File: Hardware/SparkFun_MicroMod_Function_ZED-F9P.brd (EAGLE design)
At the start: 160 x 100 mm, 0 parts

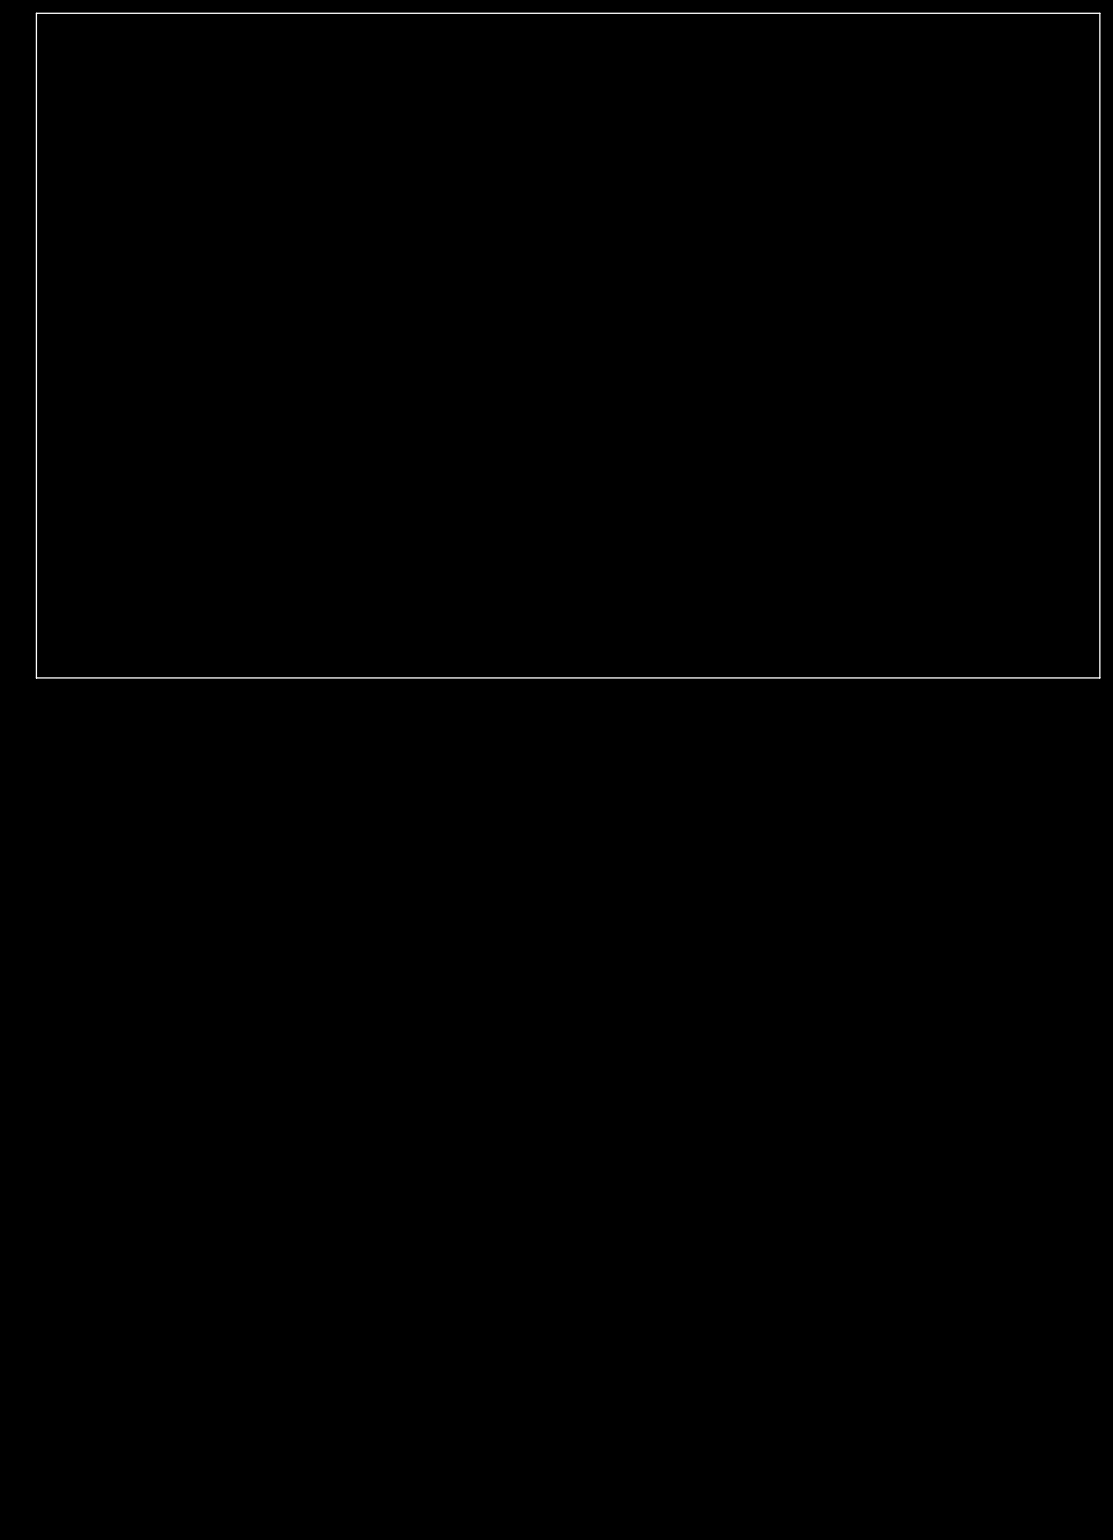
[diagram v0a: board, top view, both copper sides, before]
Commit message: Added EEPROM. Added LEDs. Added Module. Added Backup Battery. Added USB-C connector. Added Qwiic connector. Added GNSS App Note.
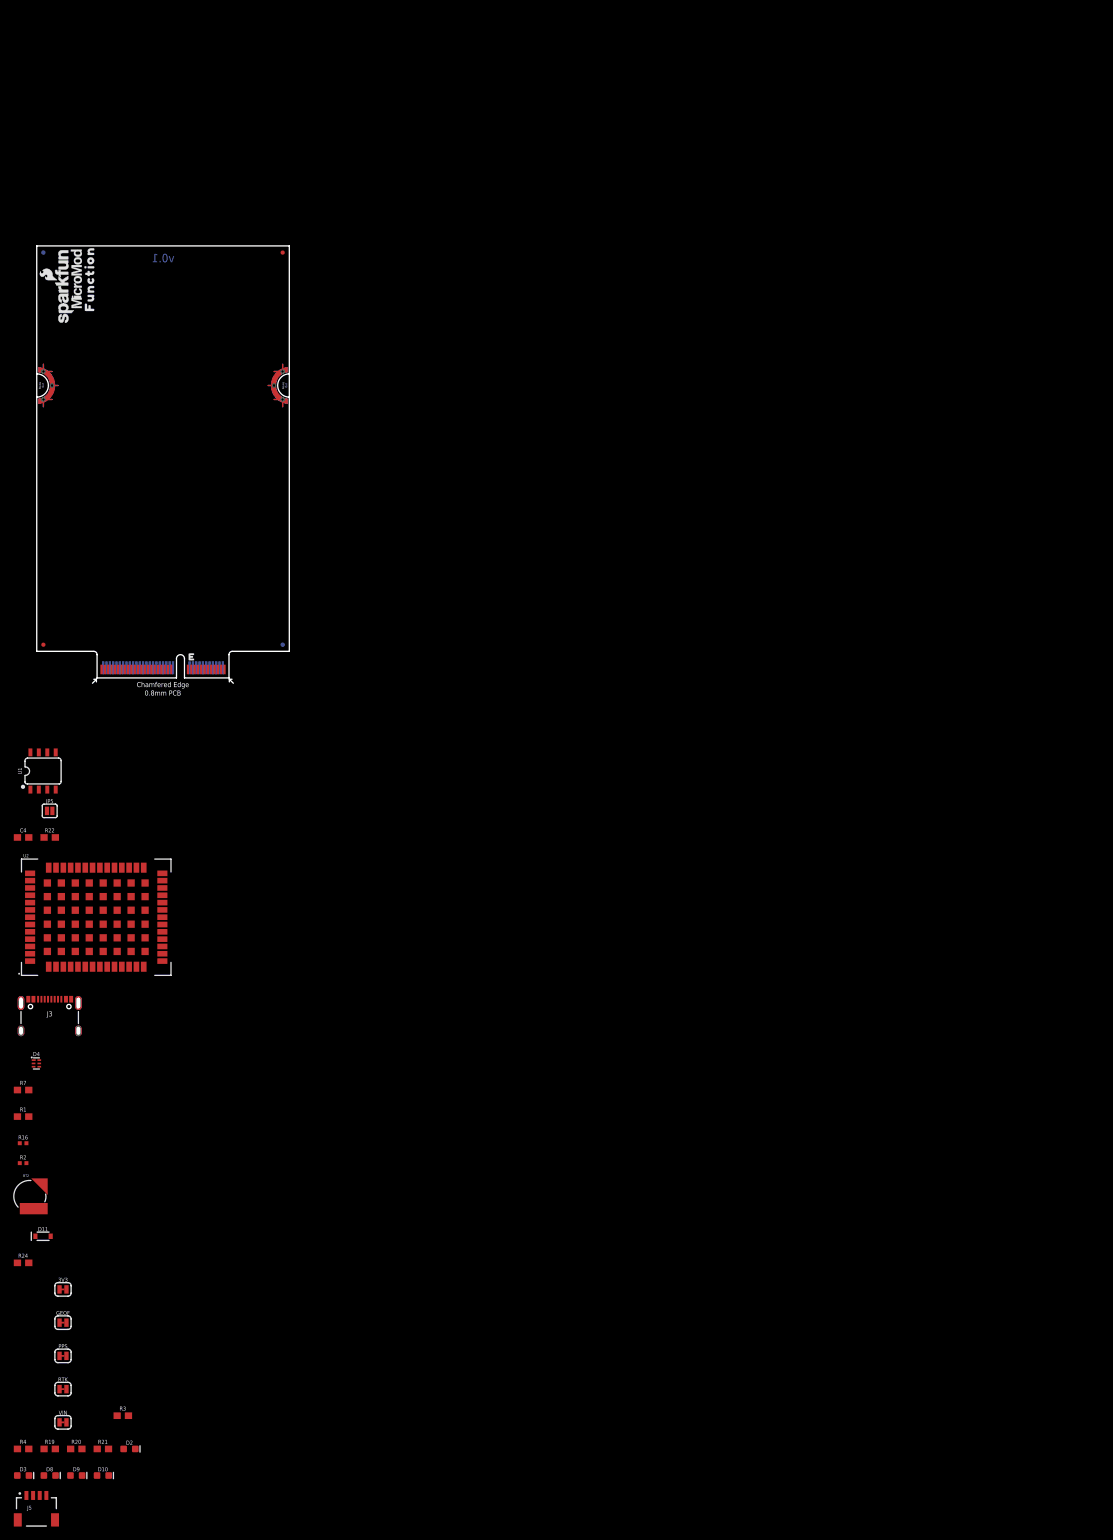
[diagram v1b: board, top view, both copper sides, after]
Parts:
- added 3V3, GEOF, PPS, RTK, VIN: JUMPER-SMT_2_NC_TRACE_SILK, SparkFun-Jumpers:SMT-JUMPER_2_NC_TRACE_SILK
- added BT2: ML414H_IV01E_BATTERY, SparkFun-Batteries:ML414H_IV01E
- added C4: 0.1uF, SparkFun-Capacitors:0603
- added D10, D8, D9: BLUE, SparkFun-LED:LED-0603
- added D11: 0.5A/40V/420mV, SparkFun-DiscreteSemi:SOD-323
- added D2, D3: RED, SparkFun-LED:LED-0603
- added D4: PRTR5V0U2F, SparkFun-IC-Power:SOT886
- added FD1, FD2, FD3, FD4: FIDUCIALUFIDUCIAL, SparkFun-Aesthetics:FIDUCIAL-MICRO
- added FRAME1: FRAME-LEDGER, SparkFun-Aesthetics:CREATIVE_COMMONS
- added J11: MICROMOD_STANDARD, SparkFun-MicroMod-Function:M.2-CARD-E-22_FUNCTION_STANDARD
- added J3: (no value), SparkFun-Connectors:USB-C-16P-2LAYER-PADS
- added J5: QWIIC_RA, SparkFun-Connectors:JST04_1MM_RA
- added JP5: JUMPER-SMT_2_NO_SILK, SparkFun-Jumpers:SMT-JUMPER_2_NO_SILK
- added LOGO1, LOGO4: SFE_LOGO_NAME_FLAME.1_INCH, SparkFun-Aesthetics:SFE_LOGO_NAME_FLAME_.1
- added LOGO2: SPECIAL_INSTRUCTIONS-ORDERING, SparkFun-Aesthetics:ORDERING_INSTRUCTIONS
- added LOGO3: OSHW-LOGOMINI, SparkFun-Aesthetics:OSHW-LOGO-MINI
- added R1, R7: 5.1k, SparkFun-Resistors:0603
- added R16, R2: 27OHM, SparkFun-Resistors:0402-TIGHT
- added R19, R20, R21, R3, R4: 1k, SparkFun-Resistors:0603
- added R22: 10k, SparkFun-Resistors:0603@1
- added R24: 3.3k, SparkFun-Resistors:0603
- added U$26, U$27: (no value), output:FUNCTION0
- added U$37, U$63: (no value), SparkFun-MicroMod:MICROMOD_LOGO_.35
- added U1: EEPROM, SparkFun-IC-Memory:SO08
- added U2: U-BLOX_ZED-F9P, SparkFun-GPS:ZED-F9P
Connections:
- new net 3.3V: C4.1, D11.A, D2.A, J11.73, J5.2, R22.1, U1.8
- new net A0: J11.36, U1.1
- new net A1: J11.34, U1.2
- new net A2: J11.32, U1.3
- new net EWP: J11.40, JP5.2, R22.2, U1.7
- new net GEO_STAT: D10.A
- new net GND: 3V3.2, BT2.-, C4.2, D4.2, GEOF.1, J11.1, J11.33, J11.39, J11.45, J11.75, J11.GND1, J11.GND2, J11.GND3, J11.GND4, J11.GND5, J11.GND6, J3.GND, J3.GND2, J5.1, JP5.1, PPS.1, R1.1, R7.1, RTK.1, U1.4, U2.1, U2.100, U2.101, U2.102, U2.12, U2.14, U2.3, U2.32, U2.37, U2.41, U2.48, U2.55, U2.56, U2.57, U2.58, U2.59, U2.60, U2.61, U2.62, U2.63, U2.64, U2.65, U2.66, U2.67, U2.68, U2.69, U2.70, U2.71, U2.72, U2.73, U2.74, U2.75, U2.76, U2.77, U2.78, U2.79, U2.80, U2.81, U2.82, U2.83, U2.84, U2.85, U2.86, U2.87, U2.88, U2.89, U2.90, U2.91, U2.92, U2.93, U2.94, U2.95, U2.96, U2.97, U2.98, U2.99, VIN.2
- new net N$1: D4.1, J3.A6, J3.B6
- new net N$10: R4.1, VIN.1
- new net N$11: D3.C, R4.2
- new net N$2: D4.3, J3.A7, J3.B7
- new net N$27: PPS.2, R19.1
- new net N$28: D8.C, R19.2
- new net N$29: D9.C, R20.2
- new net N$3: J3.B5, R7.2
- new net N$32: D11.C, R24.2
- new net N$4: J3.A5, R1.2
- new net N$45: GEOF.2, R21.1
- new net N$46: D10.C, R21.2
- new net N$5: D4.6, R16.1
- new net N$6: D4.4, R2.1
- new net N$7: D2.C, R3.2
- new net N$8: R20.1, RTK.2
- new net N$9: 3V3.1, R3.1
- new net PPS: D8.A
- new net PWR_EN: J11.71
- new net RTK_STAT: D9.A
- new net SCL/SCK: J11.21, J5.4, U1.6
- new net SDA/!CS!: J11.19, J5.3, U1.5
- new net SPI_CIPO: J11.7
- new net SPI_COPI: J11.5
- new net SPI_SCK: J11.3
- new net VCC: J11.72, J11.74
- new net VIN: D3.A
- new net V_BATT: BT2.+, R24.1
- new net V_USB: D4.5, J3.VBUS1, J3.VBUS2
- new net ZED_USB_N: R2.2
- new net ZED_USB_P: R16.2
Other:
- board size 160 x 100 mm -> 38 x 65 mm
- board text added: "2-Layer"
- board text added: "A. Brudner"
- board text added: "Beveled Edge"
- board text added: "Board Thickness is 0.8mm"
- board text added: "Dimensions are in mm"
- board text added: "ENIG Finish"
- board text added: "v0.1"

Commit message: Added I2C protection for ZED_F9P
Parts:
- added R5: 10k, SparkFun-Resistors:0603
- added U3: (no value), SparkFun-IC-Comms:SOP50P310X90-8L
- R22: device SparkFun-Resistors:0603@1 -> SparkFun-Resistors:0603
- moved GEOF 213.6 mm to (-0.52, -310.6)
- moved PPS 195.9 mm to (-0.52, -297.9)
- moved RTK 178.2 mm to (-0.52, -285.1)
- moved 3V3 167.8 mm to (-0.52, -259.8)
- moved VIN 160.5 mm to (-0.52, -272.4)
- moved R21 131.5 mm to (-0.85, -247.1)
- moved R22 121.5 mm to (-0.85, -145.4)
- moved R20 118.5 mm to (-0.85, -234.3)
- moved R19 105.7 mm to (-0.85, -221.7)
- moved R1 104.9 mm to (-0.85, -170.8)
- moved R7 96.2 mm to (-0.85, -158.2)
- moved R24 95.6 mm to (-0.85, -183.6)
- moved R4 93.0 mm to (-0.85, -208.9)
- moved R3 86.4 mm to (-0.85, -196.2)
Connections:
- new net ZED_SCL/SCK: U2.45, U3.6
- new net ZED_SDA/!CS!: U2.44, U3.5
- net 3.3V: now also R5.2, U3.2, U3.7, U3.8
- net GND: now also R5.1, U3.1
- net SCL/SCK: now also U3.3
- net SDA/!CS!: now also U3.4

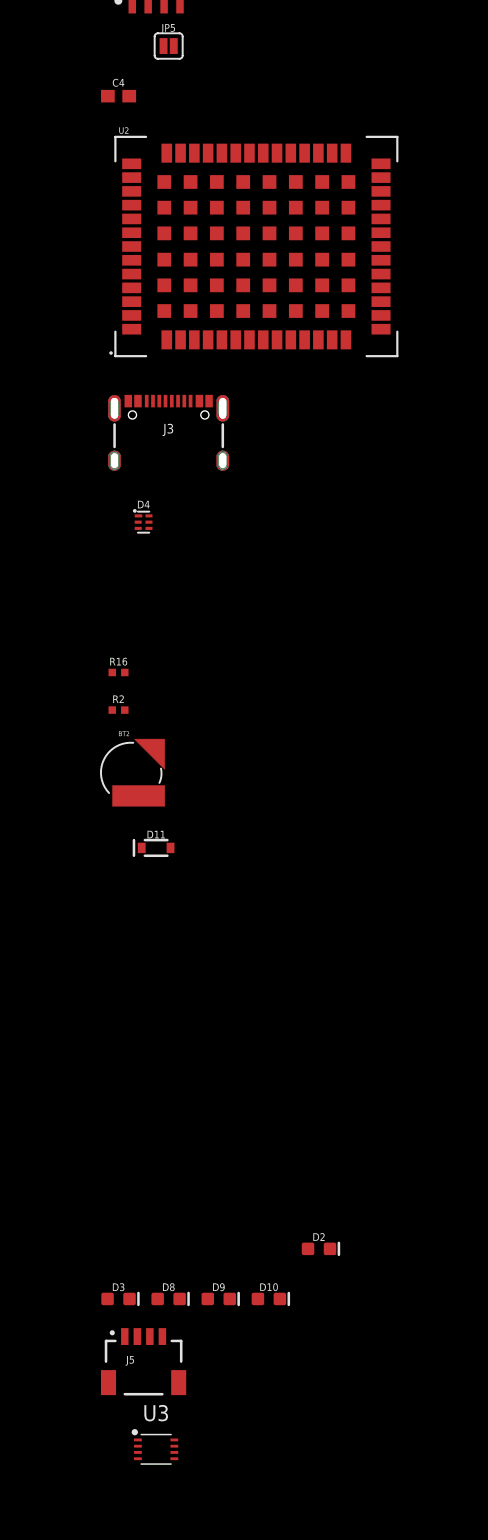
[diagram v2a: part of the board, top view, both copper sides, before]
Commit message: Created local library. Added ZED-F9P to sch.
Created Local library.
Added inverter to lib.
Added octal buffer to lib.
Added modified ZED-F9P to lib.
Added ZED-F9P to sch.
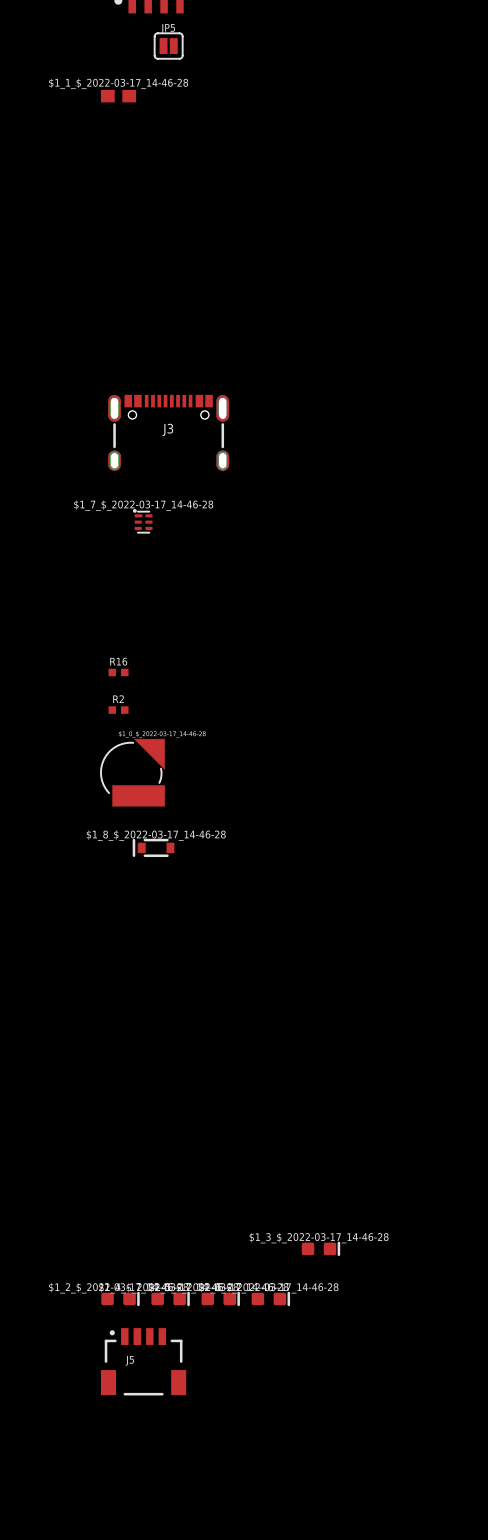
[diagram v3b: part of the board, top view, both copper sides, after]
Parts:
- removed U2: U-BLOX_ZED-F9P, SparkFun-GPS:ZED-F9P
- removed U3: (no value), SparkFun-IC-Comms:SOP50P310X90-8L
- renumbered BT2 to $1_0_$_2022-03-17_14-46-28, C4 to $1_1_$_2022-03-17_14-46-28, D10 to $1_6_$_2022-03-17_14-46-28, D11 to $1_8_$_2022-03-17_14-46-28, D2 to $1_3_$_2022-03-17_14-46-28, D3 to $1_2_$_2022-03-17_14-46-28, D4 to $1_7_$_2022-03-17_14-46-28, D8 to $1_4_$_2022-03-17_14-46-28, D9 to $1_5_$_2022-03-17_14-46-28, FD1 to $1_9_$_2022-03-17_14-46-28, FD2 to $1_11_$_2022-03-17_14-46-28, FD3 to $1_12_$_2022-03-17_14-46-28, FD4 to $1_10_$_2022-03-17_14-46-28, FRAME1 to $1_13_$_2022-03-17_14-46-28
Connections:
- removed net ZED_SCL/SCK: U2.45, U3.6
- removed net ZED_SDA/!CS!: U2.44, U3.5
- net 3.3V: no longer U3.2, U3.7, U3.8
- net GND: no longer U2.1, U2.100, U2.101, U2.102, U2.12, U2.14, U2.3, U2.32, U2.37, U2.41, U2.48, U2.55, U2.56, U2.57, U2.58, U2.59, U2.60, U2.61, U2.62, U2.63, U2.64, U2.65, U2.66, U2.67, U2.68, U2.69, U2.70, U2.71, U2.72, U2.73, U2.74, U2.75, U2.76, U2.77, U2.78, U2.79, U2.80, U2.81, U2.82, U2.83, U2.84, U2.85, U2.86, U2.87, U2.88, U2.89, U2.90, U2.91, U2.92, U2.93, U2.94, U2.95, U2.96, U2.97, U2.98, U2.99, U3.1
- net SCL/SCK: no longer U3.3
- net SDA/!CS!: no longer U3.4

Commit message: Filled out octal buffers, labeled nets. Modified inverter sch symbol.
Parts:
- removed $1_0_$_2022-03-17_14-46-28: ML414H_IV01E_BATTERY, SparkFun-Batteries:ML414H_IV01E
- removed $1_1_$_2022-03-17_14-46-28: 0.1uF, SparkFun-Capacitors:0603
- removed $1_2_$_2022-03-17_14-46-28, $1_3_$_2022-03-17_14-46-28: RED, SparkFun-LED:LED-0603
- removed $1_4_$_2022-03-17_14-46-28, $1_5_$_2022-03-17_14-46-28, $1_6_$_2022-03-17_14-46-28: BLUE, SparkFun-LED:LED-0603
- removed $1_7_$_2022-03-17_14-46-28: PRTR5V0U2F, SparkFun-IC-Power:SOT886
- removed $1_8_$_2022-03-17_14-46-28: 0.5A/40V/420mV, SparkFun-DiscreteSemi:SOD-323
- removed J5: QWIIC_RA, SparkFun-Connectors:JST04_1MM_RA
- removed R19, R21: 1k, SparkFun-Resistors:0603
- removed R22: 10k, SparkFun-Resistors:0603
- removed RTK: JUMPER-SMT_2_NC_TRACE_SILK, SparkFun-Jumpers:SMT-JUMPER_2_NC_TRACE_SILK
- added BT1: ML414H_IV01E_BATTERY, SparkFun-Batteries:ML414H_IV01E
- added C1: 10pF, SparkFun-Capacitors:0603
- added C2: 0.1uF, SparkFun-Capacitors:0603
- added D1, D2: RED, SparkFun-LED:LED-0603
- added D3, D4, D5: BLUE, SparkFun-LED:LED-0603
- added D6: PRTR5V0U2F, SparkFun-IC-Power:SOT886
- added D7: 0.5A/40V/420mV, SparkFun-DiscreteSemi:SOD-323
- added J1: (no value), SparkFun-Connectors:USB-C-16P-2LAYER-PADS
- added JP1: JUMPER-SMT_2_NO_SILK, SparkFun-Jumpers:SMT-JUMPER_2_NO_SILK
- added JP7: NC, SparkFun-Jumpers:SMT-JUMPER_2_NC_TRACE_SILK
- added R10, R9: 27OHM, SparkFun-Resistors:0402-TIGHT
- added R12: 220k, SparkFun-Resistors:0603
- added R13, R14, R15: 1.5k, SparkFun-Resistors:0603
- added R17: 10k, SparkFun-Resistors:0603
- added R8: 5.1k, SparkFun-Resistors:0603
- added U2: PCA9306DCUR, MicroMod_Function_GNSS_ublox_ZED-F9P:VSSOP-8_DCU
- added U3: U-BLOX_ZED-F9P, MicroMod_Function_GNSS_ublox_ZED-F9P:ZED-F9P
- added U4, U5: 74LVC541ABQ, MicroMod_Function_GNSS_ublox_ZED-F9P:DHVQFN20
- added U6: SN74AUP1T04DCK, MicroMod_Function_GNSS_ublox_ZED-F9P:SC-70-5_DCK
- J3: value (none) -> QWIIC_RA; device SparkFun-Connectors:USB-C-16P-2LAYER-PADS -> SparkFun-Connectors:JST04_1MM_RA
- JP5: value JUMPER-SMT_2_NO_SILK -> JUMPER-SMT_2_NC_TRACE_SILK; device SparkFun-Jumpers:SMT-JUMPER_2_NO_SILK -> SparkFun-Jumpers:SMT-JUMPER_2_NC_TRACE_SILK
- R1: value 5.1k -> 10k
- R16: value 27OHM -> 1.5k; device SparkFun-Resistors:0402-TIGHT -> SparkFun-Resistors:0603
- R2: value 27OHM -> 5.1k; device SparkFun-Resistors:0402-TIGHT -> SparkFun-Resistors:0603
- R5: value 10k -> 1k
- R7: value 5.1k -> 1k
- moved R16 314.5 mm to (-19.0, -384.0)
- moved JP5 265.2 mm to (-0.52, -285.1)
- moved R5 93.4 mm to (-0.85, -221.7)
- moved R7 88.9 mm to (-0.85, -247.1)
- moved R2 85.2 mm to (-0.85, -158.2)
- moved J3 75.0 mm to (0.00, -123.0)
- moved R1 25.4 mm to (-0.85, -145.4)
- moved R3 12.7 mm to (-0.85, -208.9)
- moved R4 12.7 mm to (-0.85, -196.2)
- renumbered $1_10_$_2022-03-17_14-46-28 to FD2, $1_11_$_2022-03-17_14-46-28 to FD3, $1_12_$_2022-03-17_14-46-28 to FD4, $1_13_$_2022-03-17_14-46-28 to FRAME1, $1_9_$_2022-03-17_14-46-28 to FD1, 3V3 to JP3, GEOF to JP6, J11 to J2, PPS to JP4, R20 to R6, R24 to R11, VIN to JP2
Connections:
- removed net SPI_CIPO: J2.7
- removed net SPI_COPI: J2.5
- removed net SPI_SCK: J2.3
- new net !RESET!: U4.P$4
- new net !SAFEBOOT!: U4.P$5
- new net !SHORT!: U4.P$8
- new net ANT_DETECT: U4.P$7
- new net ANT_OFF: U5.P$18
- new net EXTINT: U4.P$6
- new net IO_!OE!: U4.P$1, U4.P$19, U5.P$1, U5.P$19, U6.P$4
- new net N$12: C1.1, R12.1, U2.P$7, U2.P$8
- new net N$13: C2.1, U1.8
- new net N$14: U6.P$2, U6.P$5
- new net N$16: JP7.2
- new net N$18: J2.38
- new net N$19: J2.47
- new net N$21: J2.51
- new net N$22: J2.53
- new net N$23: J2.55
- new net N$24: JP7.1, R17.2, U4.P$9
- new net N$25: J2.57
- new net N$26: J2.59
- new net N$30: J2.61
- new net N$31: J2.70
- new net N$33: J2.37
- new net N$34: J2.35
- new net N$35: J2.18
- new net N$36: J2.16
- new net N$37: J2.43
- new net N$38: J2.41
- new net N$39: U4.P$20
- new net N$42: U5.P$20
- new net N$69: U3.38
- new net N$73: U3.7
- new net N$74: U3.2
- new net N$77: U3.33, U3.34
- new net RX/COPI: J2.15, J2.5, U4.P$3
- new net RX2/RTCM: U4.P$2
- new net TIMEPULSE: U5.P$12
- new net TX/CIPO: J2.13, J2.7, U5.P$14
- new net TX2/RTCM: U5.P$15
- new net TX_READY: J2.23, U5.P$13
- new net ZED_!ANT_SHORT!: U3.6
- new net ZED_!RESET!: U3.49, U4.P$16
- new net ZED_!SAFEBOOT!: U3.50, U4.P$15
- new net ZED_!SHORT!: U4.P$12
- new net ZED_ANT_DETECT: U3.4, U4.P$13
- new net ZED_ANT_OFF: U3.5, U5.P$2
- new net ZED_DSEL: U3.47, U4.P$11
- new net ZED_EXTINT: U3.51, U4.P$14
- new net ZED_GEO_STAT: U3.19, U5.P$3
- new net ZED_RTK_STAT: U3.20, U5.P$4
- new net ZED_RX/COPI: U3.43, U4.P$17
- new net ZED_RX2/RTCM: U3.26, U4.P$18
- new net ZED_SCL/SCK: R14.1, U2.P$6, U3.45
- new net ZED_SDA/!CS!: R13.1, U2.P$5, U3.44
- new net ZED_TIMEPULSE: U3.53, U5.P$8
- new net ZED_TX/CIPO: U3.42, U5.P$6
- new net ZED_TX2/RTCM: U3.27, U5.P$5
- new net ZED_TX_READY: U3.46, U5.P$7
- net 3.3V: now also D2.A, D7.A, J3.2, R1.1, R12.2, R13.2, R14.2, R15.2, R16.2, U2.P$2; no longer $1_1_$_2022-03-17_14-46-28.1, $1_3_$_2022-03-17_14-46-28.A, $1_8_$_2022-03-17_14-46-28.A, J5.2, R22.1, R5.2, U1.8
- net EWP: now also JP1.2, R1.2; no longer JP5.2, R22.2
- net GEO_STAT: now also D5.A, U5.P$17; no longer $1_6_$_2022-03-17_14-46-28.A
- net GND: now also BT1.-, C1.2, C2.2, D6.2, J1.GND, J1.GND2, J1.SHLD1, J1.SHLD2, J1.SHLD3, J1.SHLD4, J3.1, JP1.1, R17.1, R2.1, R8.1, U2.P$1, U3.1, U3.100, U3.101, U3.102, U3.12, U3.14, U3.3, U3.32, U3.37, U3.41, U3.48, U3.55, U3.56, U3.57, U3.58, U3.59, U3.60, U3.61, U3.62, U3.63, U3.64, U3.65, U3.66, U3.67, U3.68, U3.69, U3.70, U3.71, U3.72, U3.73, U3.74, U3.75, U3.76, U3.77, U3.78, U3.79, U3.80, U3.81, U3.82, U3.83, U3.84, U3.85, U3.86, U3.87, U3.88, U3.89, U3.90, U3.91, U3.92, U3.93, U3.94, U3.95, U3.96, U3.97, U3.98, U3.99, U4.P$10, U4.P$21, U5.P$10, U5.P$11, U5.P$21, U5.P$9, U6.P$3; no longer $1_0_$_2022-03-17_14-46-28.-, $1_1_$_2022-03-17_14-46-28.2, $1_7_$_2022-03-17_14-46-28.2, J3.GND, J3.GND2, J5.1, R1.1, R5.1, R7.1, RTK.1
- net N$1: now also D6.1, J1.A6, J1.B6; no longer $1_7_$_2022-03-17_14-46-28.1, J3.A6, J3.B6
- net N$10: now also R3.1; no longer R4.1
- net N$11: now also D1.C, R3.2; no longer $1_2_$_2022-03-17_14-46-28.C, R4.2
- net N$2: now also D6.3, J1.A7, J1.B7; no longer $1_7_$_2022-03-17_14-46-28.3, J3.A7, J3.B7
- net N$27: now also R5.1; no longer R19.1
- net N$28: now also D3.C, R5.2; no longer $1_4_$_2022-03-17_14-46-28.C, R19.2
- net N$29: now also D4.C; no longer $1_5_$_2022-03-17_14-46-28.C
- net N$3: now also J1.B5, R2.2; no longer J3.B5, R7.2
- net N$32: now also D7.C; no longer $1_8_$_2022-03-17_14-46-28.C
- net N$4: now also J1.A5, R8.2; no longer J3.A5, R1.2
- net N$45: now also R7.1; no longer R21.1
- net N$46: now also D5.C, R7.2; no longer $1_6_$_2022-03-17_14-46-28.C, R21.2
- net N$5: now also D6.6, R9.1; no longer $1_7_$_2022-03-17_14-46-28.6, R16.1
- net N$6: now also D6.4, R10.1; no longer $1_7_$_2022-03-17_14-46-28.4, R2.1
- net N$7: now also D2.C, R4.2; no longer $1_3_$_2022-03-17_14-46-28.C, R3.2
- net N$8: now also JP5.2; no longer RTK.2
- net N$9: now also R4.1; no longer R3.1
- net PPS: now also D3.A; no longer $1_4_$_2022-03-17_14-46-28.A
- net RTK_STAT: now also D4.A, U5.P$16; no longer $1_5_$_2022-03-17_14-46-28.A
- net SCL/SCK: now also J2.3, J3.4, R16.1, U2.P$3; no longer J5.4
- net SDA/!CS!: now also J2.49, J3.3, R15.1, U2.P$4; no longer J5.3
- net VIN: now also D1.A; no longer $1_2_$_2022-03-17_14-46-28.A
- net V_BATT: now also BT1.+, U3.36; no longer $1_0_$_2022-03-17_14-46-28.+
- net V_USB: now also D6.5, J1.VBUS1, J1.VBUS2; no longer $1_7_$_2022-03-17_14-46-28.5, J3.VBUS1, J3.VBUS2
- net ZED_USB_N: now also R10.2, U3.39; no longer R2.2
- net ZED_USB_P: now also R9.2, U3.40; no longer R16.2
